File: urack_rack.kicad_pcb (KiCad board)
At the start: 2 copper layers, 250 x 250 mm, 9 parts

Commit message: Add linear voltage reguator make PCB
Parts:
- added C10: CP, Capacitor_SMD:CP_Elec_6.3x7.7, F.Cu at (40.4, 37.6)
- added C11: CP, Capacitor_SMD:CP_Elec_6.3x7.7, F.Cu at (40.4, 25.8)
- added C12: C, Capacitor_SMD:C_0603_1608Metric_Pad1.05x0.95mm_HandSolder, F.Cu at (46.0, 37.3)
- added C13: C, Capacitor_SMD:C_0603_1608Metric_Pad1.05x0.95mm_HandSolder, F.Cu at (46.2, 24.1)
- added C14: C, Capacitor_SMD:C_0603_1608Metric_Pad1.05x0.95mm_HandSolder, F.Cu at (67.0, 50.4)
- added C15: C, Capacitor_SMD:C_0603_1608Metric_Pad1.05x0.95mm_HandSolder, F.Cu at (66.3, 36.6)
- added C16: C, Capacitor_SMD:C_0603_1608Metric_Pad1.05x0.95mm_HandSolder, F.Cu at (63.9, 50.5)
- added C17: C, Capacitor_SMD:C_0603_1608Metric_Pad1.05x0.95mm_HandSolder, F.Cu at (69.4, 36.6)
- added J1: Screw_Terminal_01x03, TerminalBlock_Phoenix:TerminalBlock_Phoenix_PT-1,5-3-3.5-H_1x03_P3.50mm_Horizontal, F.Cu at (26.5, 33.2)
- added U1: LM1117-5.0, Package_TO_SOT_SMD:TO-252-2, F.Cu at (55.5, 49.5)
- added U2: MC7905, Package_TO_SOT_SMD:TO-263-3_TabPin2, F.Cu at (57.7, 29.6)
- moved C9 31.1 mm to (23.7, 288.1)
- moved C3 29.2 mm to (25.0, 293.2)
- moved C7 1.90 mm to (23.7, 118.9)
- moved C8 1.90 mm to (24.7, 188.9)
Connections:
- net GNDREF renamed GND
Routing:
- net +5V: track 868.5 -> 1180.8 mm
- net GND: track 951.3 -> 998.1 mm, vias 1 -> 0
- net -5V: track 873.8 -> 918.4 mm, vias 0 -> 1
- net Net-(C11-Pad2): track 0.00 -> 42.9 mm
- net Net-(C10-Pad1): track 0.00 -> 41.2 mm
- added copper zone on F.Cu, net GND
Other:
- board size 250 x 250 mm -> 250 x 276.8 mm

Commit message: Delete LDO. New size connector
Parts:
- removed C10, C11: CP, Capacitor_SMD:CP_Elec_6.3x7.7
- removed C12, C13, C14, C15, C16, C17: C, Capacitor_SMD:C_0603_1608Metric_Pad1.05x0.95mm_HandSolder
- removed J1: Screw_Terminal_01x03, TerminalBlock_Phoenix:TerminalBlock_Phoenix_PT-1,5-3-3.5-H_1x03_P3.50mm_Horizontal
- removed U1: LM1117-5.0, Package_TO_SOT_SMD:TO-252-2
- removed U2: MC7905, Package_TO_SOT_SMD:TO-263-3_TabPin2
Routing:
- net +5V: track 1180.8 -> 897.1 mm
- net GND: track 998.1 -> 904.3 mm
- net -5V: track 918.4 -> 873.8 mm, vias 1 -> 0
- net Net-(C11-Pad2): track 42.9 -> 0.00 mm
- net Net-(C10-Pad1): track 41.2 -> 0.00 mm
- removed copper zone on F.Cu, net GND

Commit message: New version PCB. Change power connectors, add USB Type C connector Molex 105450-0101
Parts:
- removed C1, C2, C3, C4, C5, C6, C7, C8, C9: Conn_01x96_Female, footprint:pbd1x96
- added J1: Conn_01x40, footprint:pbd1x40, F.Cu at (24.7, 31.8)
- added J10: 105450-0101, footprint:MOLEX_105450-0101, F.Cu at (225.8, 134.4)
- added J11: 105450-0101, footprint:MOLEX_105450-0101, F.Cu at (47.4, 24.2)
- added J12: 105450-0101, footprint:MOLEX_105450-0101, F.Cu at (24.2, 129.7)
- added J2: Conn_01x40, footprint:pbd1x40, F.Cu at (126.7, 31.8)
- added J3: Conn_01x40, footprint:pbd1x40, F.Cu at (24.7, 104.2)
- added J4: Conn_01x40, footprint:pbd1x40, F.Cu at (126.3, 104.2)
- added J5: Conn_02x40_Odd_Even, footprint:pbd2x40, F.Cu at (24.7, 87.7)
- added J6: Conn_02x40_Odd_Even, footprint:pbd2x40, F.Cu at (126.3, 87.7)
- added J7: Conn_02x40_Odd_Even, footprint:pbd2x40, F.Cu at (24.7, 160.1)
- added J8: Conn_02x40_Odd_Even, footprint:pbd2x40, F.Cu at (126.3, 160.1)
- added J9: 105450-0101, footprint:MOLEX_105450-0101, F.Cu at (202.7, 24.2)
- added R1: 5K1, footprint:r0603, F.Cu at (211.2, 41.2)
- added R2: 5K1, footprint:r0603, F.Cu at (201.8, 41.0)
- added R3: 5K1, footprint:r0603, F.Cu at (206.2, 127.6)
- added R4: 5K1, footprint:r0603, F.Cu at (209.1, 134.2)
- added R5: 5K1, footprint:r0603, F.Cu at (54.5, 28.0)
- added R6: 5K1, footprint:r0603, F.Cu at (56.6, 28.1)
- added R7: 5K1, footprint:r0603, F.Cu at (45.8, 127.4)
- added R8: 5K1, footprint:r0603, F.Cu at (45.8, 133.6)
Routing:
- net +5V: track 897.1 -> 0.00 mm
- net -5V: track 873.8 -> 0.00 mm
- net GND: track 904.3 -> 408.1 mm
- net +9V: track 0.00 -> 481.4 mm
- net -9V: track 0.00 -> 408.1 mm
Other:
- board size 250 x 276.8 mm -> 210 x 153.2 mm

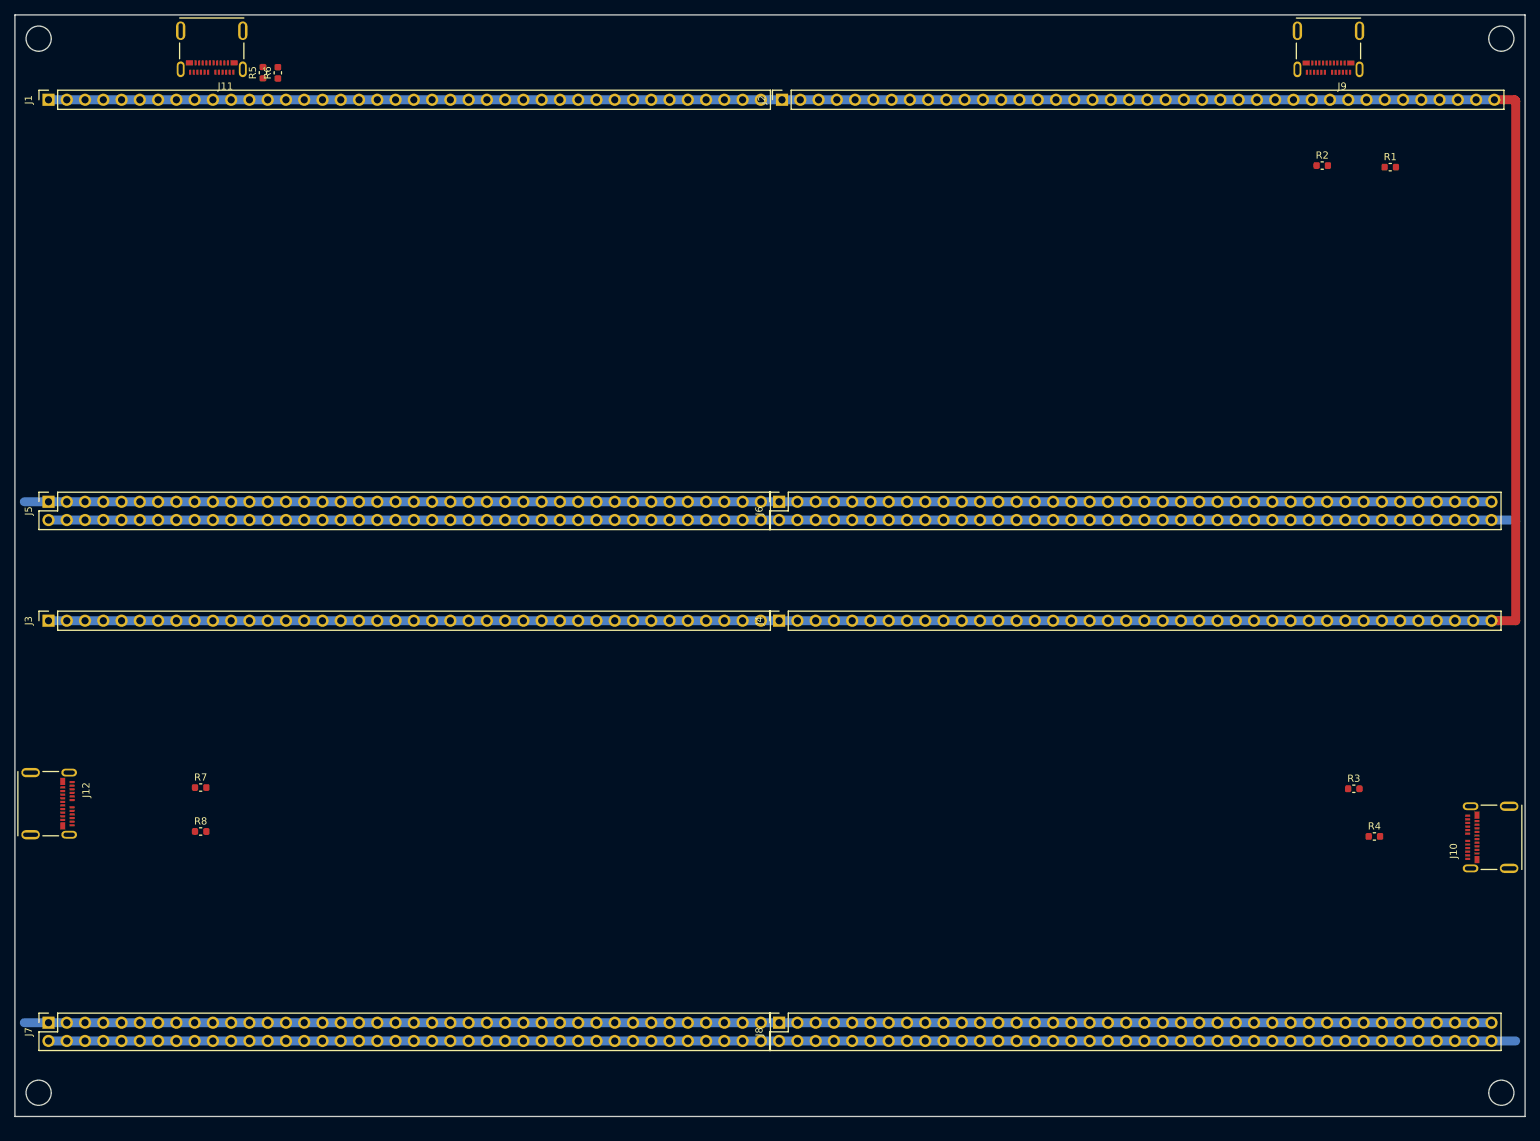
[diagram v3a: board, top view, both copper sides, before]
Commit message: board dimensions changed
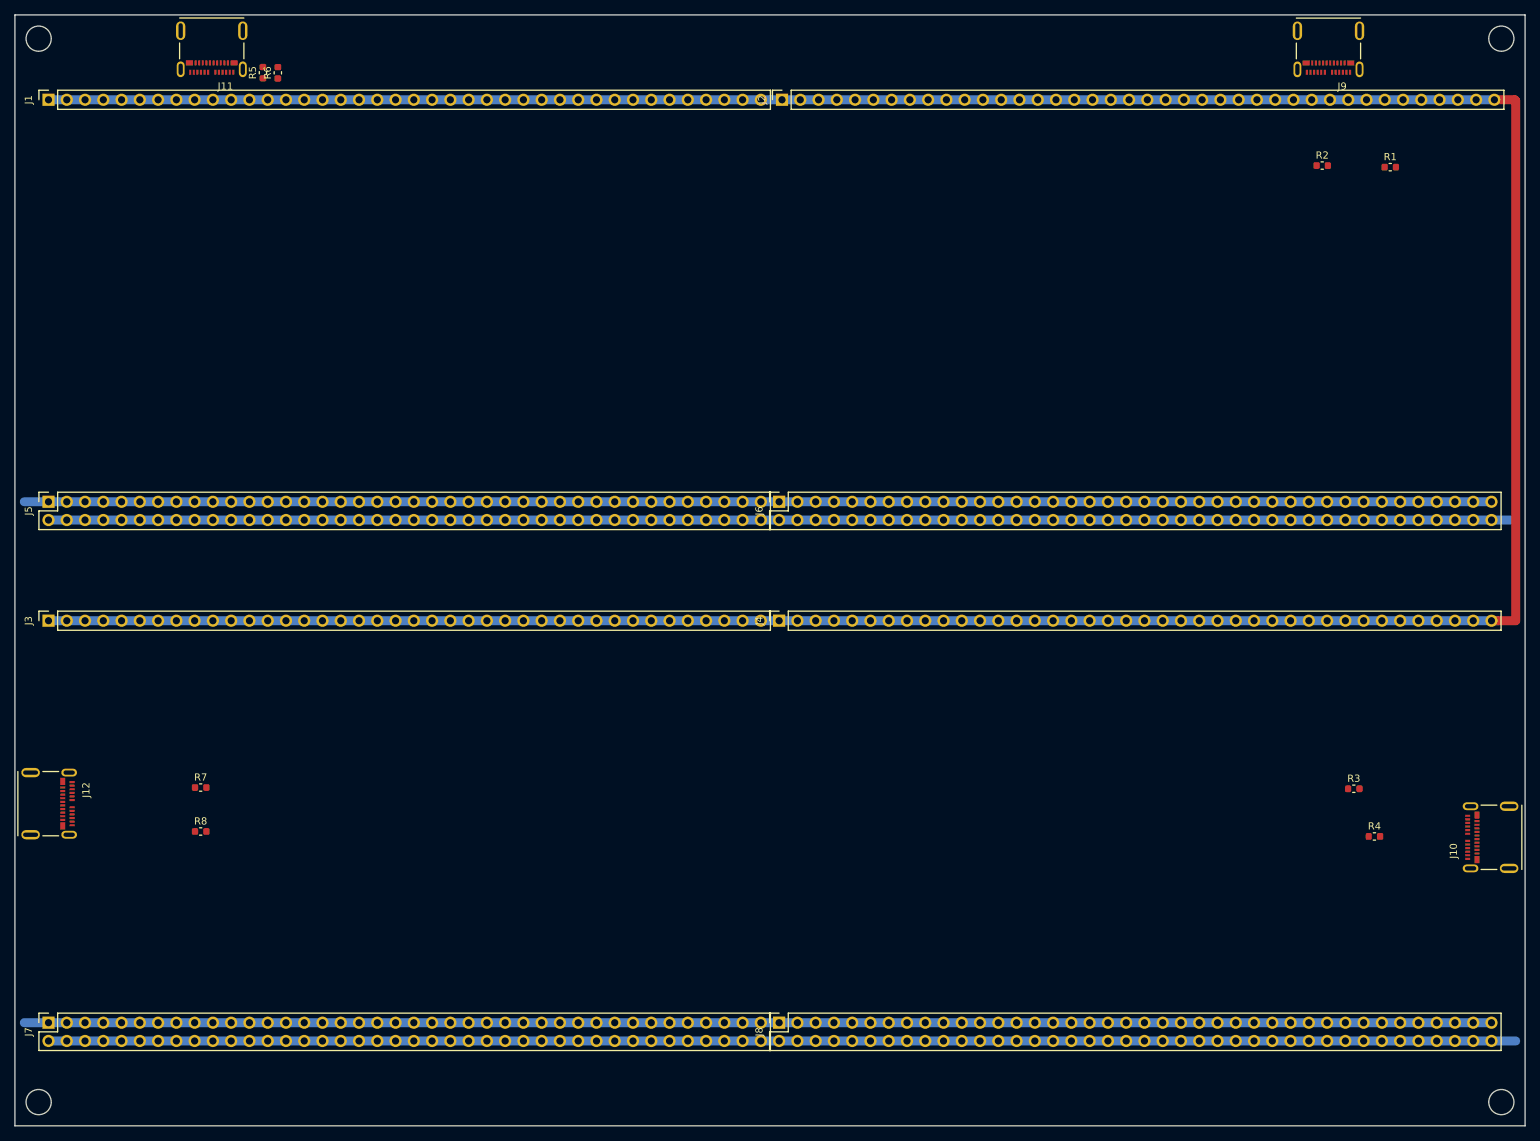
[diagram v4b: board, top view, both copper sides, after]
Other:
- board size 210 x 153.2 mm -> 210 x 154.5 mm
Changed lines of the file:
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@@
     )
   )
-  (module footprint:pbd2x40 locked (layer F.Cu)
+  (module footprint:pbd2x40 (layer F.Cu)
     (at 126.27 87.7 90)
     (descr "Through hole straight socket strip, 2x40, 2.54mm pitch, double cols (from Kicad 4.0.7), script generated")
@@
     )
   )
-  (module footprint:pbd2x40 locked (layer F.Cu)
+  (module footprint:pbd2x40 (layer F.Cu)
     (at 126.27 160.14 90)
     (descr "Through hole straight socket strip, 2x40, 2.54mm pitch, double cols (from Kicad 4.0.7), script generated")
@@
   )
   (gr_circle (center 226.7 23.3) (end 228.45 23.3) (layer Edge.Cuts) (width 0.15))
-  (gr_circle (center 23.3 169.88) (end 25.05 169.88) (layer Edge.Cuts) (width 0.15))
-  (gr_circle (center 226.7 169.88) (end 228.45 169.88) (layer Edge.Cuts) (width 0.15))
+  (gr_circle (center 23.3 171.18) (end 25.05 171.18) (layer Edge.Cuts) (width 0.15))
+  (gr_circle (center 226.7 171.18) (end 228.45 171.18) (layer Edge.Cuts) (width 0.15))
   (gr_circle (center 23.3 23.3) (end 25.05 23.3) (layer Edge.Cuts) (width 0.15))
-  (gr_line (start 230 173.18) (end 20 173.18) (layer Edge.Cuts) (width 0.15))
-  (gr_line (start 20 20) (end 20 173.18) (layer Edge.Cuts) (width 0.15))
-  (gr_line (start 230 20) (end 230 173.18) (layer Edge.Cuts) (width 0.15))
+  (gr_line (start 230 174.48) (end 20 174.48) (layer Edge.Cuts) (width 0.15))
+  (gr_line (start 20 20) (end 20 174.48) (layer Edge.Cuts) (width 0.15))
+  (gr_line (start 230 20) (end 230 174.48) (layer Edge.Cuts) (width 0.15))
   (gr_line (start 20 20) (end 230 20) (layer Edge.Cuts) (width 0.15))
   (segment (start 24.67 162.68) (end 225.33 162.68) (width 1.25) (layer B.Cu) (net 1) (status 30))

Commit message: Update PCB
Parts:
- moved R8 19.1 mm to (27.4, 138.5)
- moved R7 18.5 mm to (27.4, 125.9), turned to 180 degrees
- moved R3 16.5 mm to (222.6, 125.6)
- moved R2 15.7 mm to (193.7, 27.5), turned to 270 degrees
- moved R1 14.5 mm to (206.5, 27.5), turned to 90 degrees
- moved R4 14.1 mm to (222.5, 138.6), turned to 180 degrees
- moved R6 12.9 mm to (43.6, 27.4), turned to 270 degrees
- moved J9 2.66 mm to (200.0, 24.2)
- moved J11 2.63 mm to (50.0, 24.2)
- moved J12 2.51 mm to (24.2, 132.2)
- moved J10 2.17 mm to (225.8, 132.2)
- moved R5 1.97 mm to (56.4, 27.5)
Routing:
- net GND: track 408.1 -> 982.9 mm
- net -9V: track 408.1 -> 480.3 mm
- net +5V: track 0.00 -> 33.7 mm, vias 0 -> 8
- net Net-(J10-PadA5): track 0.00 -> 10.9 mm
- net Net-(J11-PadA5): track 0.00 -> 9.58 mm
- net Net-(J10-PadB5): track 0.00 -> 9.15 mm
- net Net-(J9-PadB5): track 0.00 -> 7.80 mm
- net Net-(J12-PadA5): track 0.00 -> 7.75 mm
- net Net-(J9-PadA5): track 0.00 -> 7.63 mm
- net Net-(J11-PadB5): track 0.00 -> 7.32 mm
- net Net-(J12-PadB5): track 0.00 -> 7.17 mm
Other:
- net class Default: clearance 0.6 -> 0.15; trace_width 1.25 -> 0.2; via_dia 1 -> 0.6; via_drill 0.6 -> 0.3
- rule trace_clearance: 0.6 -> 0.15
